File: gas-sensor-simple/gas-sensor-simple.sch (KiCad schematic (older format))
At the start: 31 parts, among them J1 6-pin male, J2 6-pin female, J3 8-pin male, U1 MQ-8, U10 MV5x3x, U11 MV5x3x, U12 LM393, U13 ads1x15, U14 ads1x15, U15 BME280, U2 MQ-4, U3 CO2, U4 O2, U5 7407, U6 7407, U8 MV5x3x, U9 MV5x3x

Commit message: Begin PCB layout.
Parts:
- removed J1: 6-pin male, symbol Conn_01x06_Male
- removed J2: 6-pin female, symbol Conn_01x06_Female
- added unit 2 of U12
- added unit 5 of U5
- added unit 6 of U5
- added unit 5 of U6
- added unit 6 of U6
- J1: renamed from J3; footprint (none) -> Pin_Headers:Pin_Header_Straight_1x08_Pitch2.54mm
- R1, R2, R3, R4, R5, R6, R7, R8: footprint (none) -> Resistors_THT:R_Axial_DIN0207_L6.3mm_D2.5mm_P10.16mm_Horizontal
- RV1: footprint (none) -> Potentiometers:Potentiometer_Trimmer_Piher_PT-10h5_Vertical_Px5.0mm_Py5.0mm
- TH1, TH2, TH3, TH4: footprint (none) -> Resistors_THT:R_Axial_DIN0204_L3.6mm_D1.6mm_P7.62mm_Horizontal
- U1, U2, U4: footprint (none) -> Socket_Strips:Socket_Strip_Straight_1x04_Pitch2.54mm
- U10, U11, U8, U9: footprint (none) -> Socket_Strips:Socket_Strip_Straight_1x03_Pitch2.54mm
- U12: footprint (none) -> Housings_DIP:DIP-8_W7.62mm
- U13, U14: footprint (none) -> Socket_Strips:Socket_Strip_Straight_1x10_Pitch2.54mm
- U15: footprint (none) -> Housings_DIP:DIP-12_W10.16mm
- U3: footprint (none) -> Pin_Headers:Pin_Header_Straight_1x04_Pitch2.54mm
- U5, U6: footprint (none) -> Housings_DIP:DIP-14_W7.62mm
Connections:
- wire segments 170 -> 163
- no-connect marks 6 -> 13
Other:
- note removed: "(5V)"

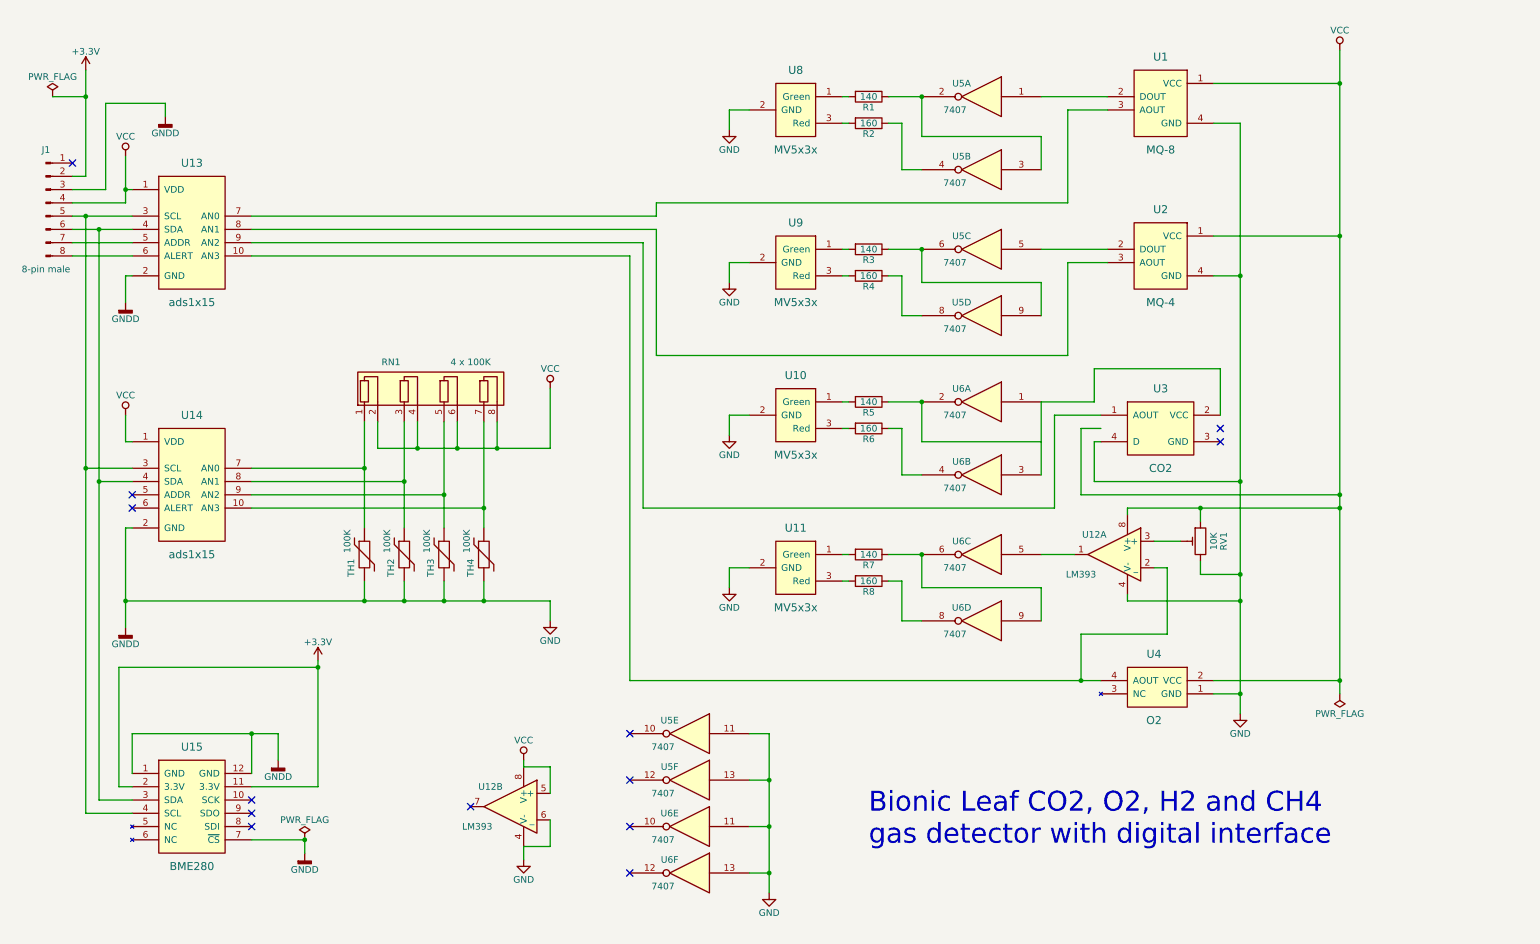
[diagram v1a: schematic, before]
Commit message: Add back headers to separate analog board from digital.
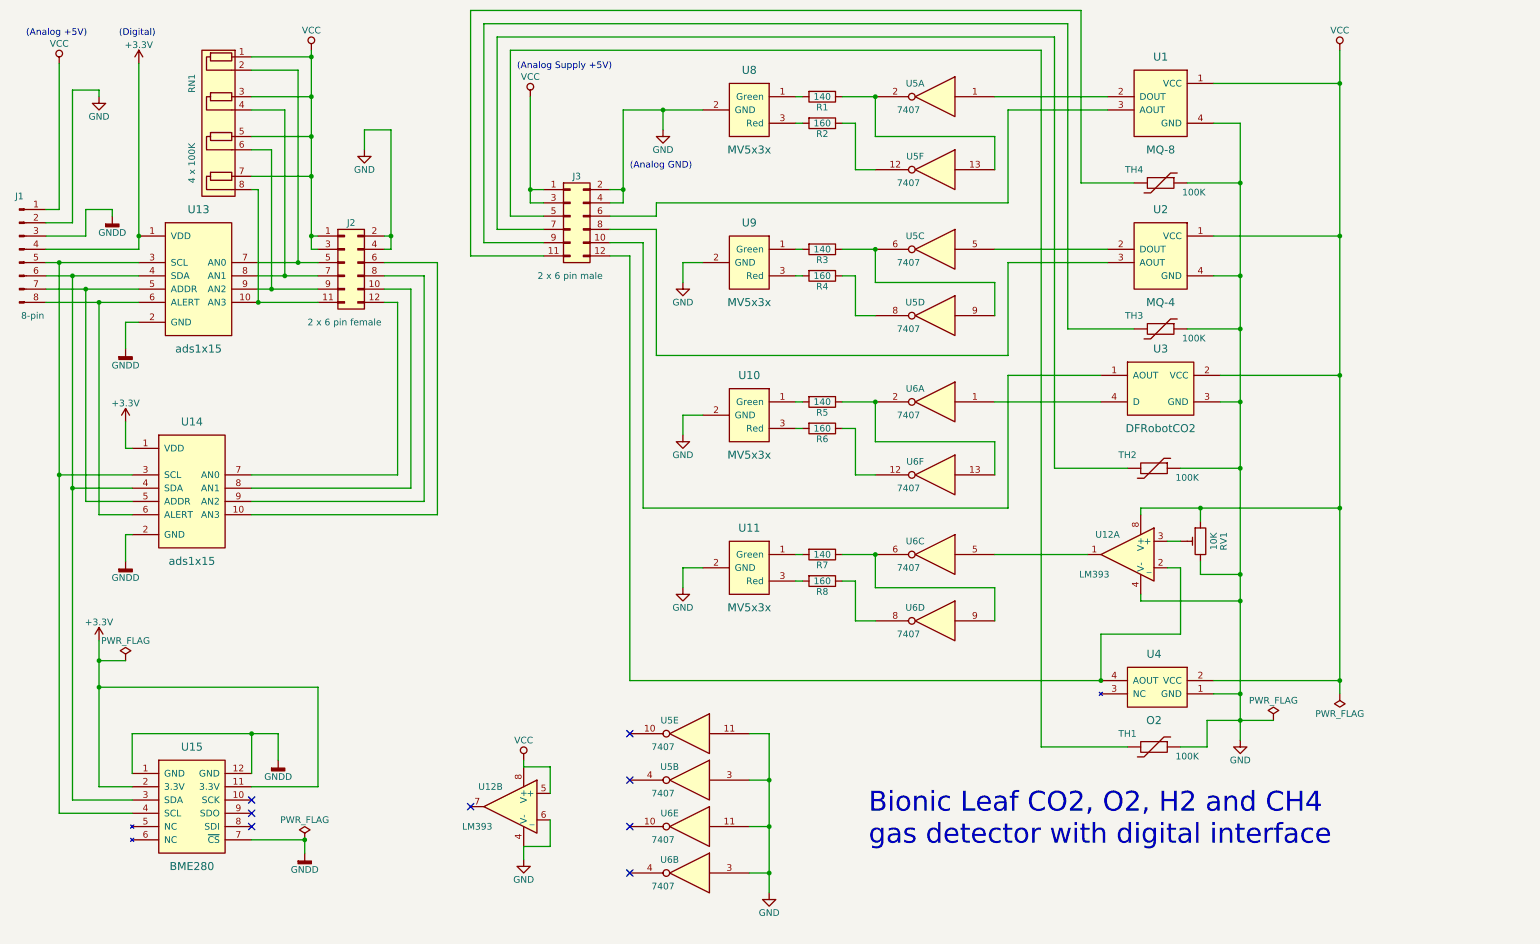
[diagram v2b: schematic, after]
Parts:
- added J2: 2 x 6 pin female, Socket_Strips:Socket_Strip_Straight_2x06_Pitch2.54mm, symbol Conn_02x06_Odd_Even
- added J3: 2 x 6 pin male, Pin_Headers:Pin_Header_Straight_2x06_Pitch2.54mm, symbol Conn_02x06_Odd_Even
- J1: value 8-pin male -> 8-pin
- TH1, TH2, TH3, TH4: footprint Resistors_THT:R_Axial_DIN0204_L3.6mm_D1.6mm_P7.62mm_Horizontal -> Socket_Strips:Socket_Strip_Straight_1x02_Pitch2.54mm
- U3: value CO2 -> DFRobotCO2; footprint Pin_Headers:Pin_Header_Straight_1x04_Pitch2.54mm -> Socket_Strips:Socket_Strip_Straight_1x04_Pitch2.54mm
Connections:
- net +3V3: now also J1.4 (Pin_4), U13.1 (VDD), U14.1 (VDD); no longer J1.2 (Pin_2)
- net GND: now also J1.2 (Pin_2), TH1.1, TH2.1, TH3.1, TH4.1, U3.3 (GND), U5.3, U6.3, J2.2 (Pin_2), J2.4 (Pin_4), J3.2 (Pin_2), J3.4 (Pin_4); no longer J1.3 (Pin_3), TH1.2, TH2.2, TH3.2, TH4.2, U13.2 (GND), U14.2 (GND), U15.1 (GND), U15.12 (GND), U15.7 (~CS~), U3.4 (D), U5.13, U6.13
- net VCC: now also J1.1 (Pin_1), RN1.1 (R1.1), RN1.3 (R2.1), RN1.5 (R3.1), RN1.7 (R4.1), U3.2 (VCC), J2.1 (Pin_1), J2.3 (Pin_3), J3.1 (Pin_1), J3.3 (Pin_3); no longer J1.4 (Pin_4), RN1.2 (R1.2), RN1.4 (R2.2), RN1.6 (R3.2), RN1.8 (R4.2), U13.1 (VDD), U14.1 (VDD)
- net at U1.3 (AOUT): now also J3.6 (Pin_6); no longer U13.7 (AN0)
- net at U2.3 (AOUT): now also J3.8 (Pin_8); no longer U13.8 (AN1)
- net at J1.7 (Pin_7), U13.5 (ADDR): now also U14.5 (ADDR)
- net at J1.8 (Pin_8), U13.6 (ALERT): now also U14.6 (ALERT)
- net at R1.1, U5.2: now also U5.13; no longer U5.3
- net at R2.1: now also U5.12; no longer U5.4
- net at R5.1, U6.2: now also U6.13
- net at R6.1: now also U6.12; no longer U6.4
- net at U12.2 (_), U4.4 (AOUT): now also J3.12 (Pin_12); no longer U13.10 (AN3)
- net at U13.9 (AN2): now also RN1.6 (R3.2), J2.9 (Pin_9); no longer U3.1 (AOUT)
- new net: U3.4 (D), U6.1
- new net: J2.11 (Pin_11), RN1.8 (R4.2), U13.10 (AN3)
- new net: J2.5 (Pin_5), RN1.2 (R1.2), U13.7 (AN0)
- new net: J2.7 (Pin_7), RN1.4 (R2.2), U13.8 (AN1)
- new net: J2.6 (Pin_6), U14.10 (AN3)
- new net: J2.12 (Pin_12), U14.7 (AN0)
- new net: J2.10 (Pin_10), U14.8 (AN1)
- new net: J2.8 (Pin_8), U14.9 (AN2)
- new net: J3.5 (Pin_5), TH1.2
- new net: J3.7 (Pin_7), TH2.2
- new net: J3.9 (Pin_9), TH3.2
- new net: J3.11 (Pin_11), TH4.2
- new net: J3.10 (Pin_10), U3.1 (AOUT)
- new net GNDD: J1.3 (Pin_3), U13.2 (GND), U14.2 (GND), U15.1 (GND), U15.12 (GND), U15.7 (~CS~)
- no-connect marks 13 -> 8
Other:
- note added: "(Analog +5V)"
- note added: "(Analog GND)"
- note added: "(Analog Supply +5V)"
- note added: "(Digital)"
- moved on the sheet: J1, R1, R2, R3, R4, R5, R6, R7, R8, RN1, TH1, TH2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

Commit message: Start adding capacitors and improve PCB layout.
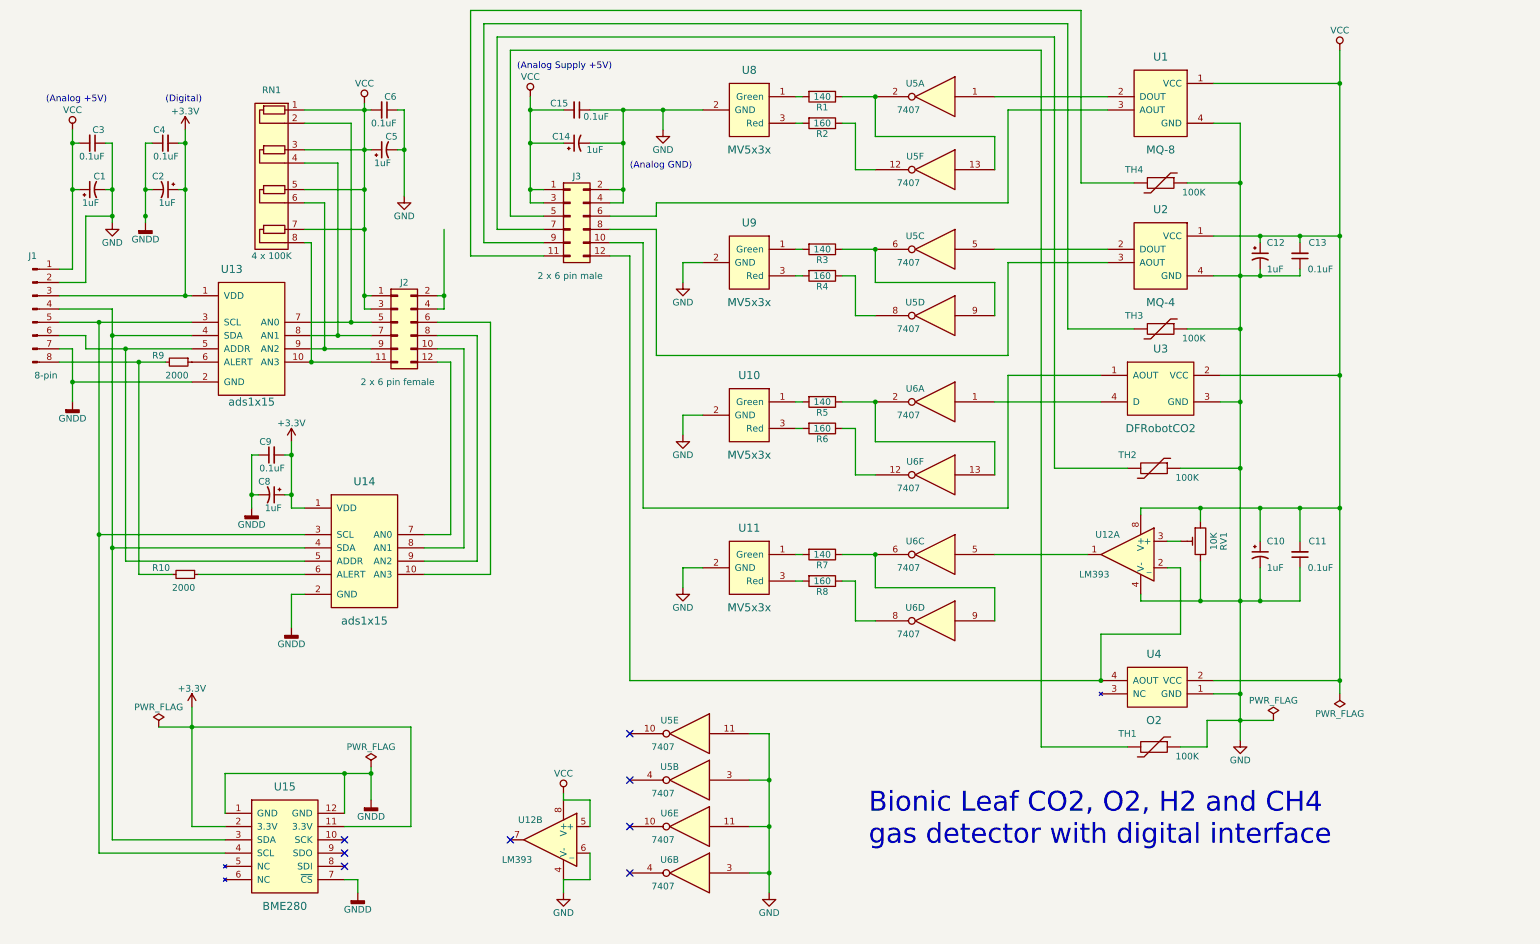
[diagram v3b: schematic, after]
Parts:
- added C1, C2, C5, C8: 1uF, Capacitors_THT:CP_Radial_D5.0mm_P2.50mm, symbol CP1_Small
- added C10, C12, C14: 1uF, symbol CP1_Small
- added C11, C13, C15: 0.1uF, symbol C_Small
- added C3, C4, C6, C9: 0.1uF, Capacitors_THT:C_Disc_D5.0mm_W2.5mm_P2.50mm, symbol C_Small
- added R10, R9: 2000, symbol R_Small
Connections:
- net +3V3: now also J1.3 (Pin_3), C2.1, C4.2, C8.1, C9.2; no longer J1.4 (Pin_4)
- net GND: now also C1.2, C10.2, C11.1, C12.2, C13.1, C14.2, C15.1, C3.1, C5.2, C6.1; no longer J2.2 (Pin_2), J2.4 (Pin_4)
- net GNDD: now also J1.7 (Pin_7), C2.2, C4.1, C8.2, C9.1; no longer J1.3 (Pin_3)
- net VCC: now also C1.1, C10.1, C11.2, C12.1, C13.2, C14.1, C15.2, C3.2, C5.1, C6.2
- net at U13.4 (SDA), U14.4 (SDA), U15.3 (SDA): now also J1.4 (Pin_4); no longer J1.6 (Pin_6)
- net at U13.5 (ADDR), U14.5 (ADDR): now also J1.6 (Pin_6); no longer J1.7 (Pin_7)
- new net: J1.8 (Pin_8), R10.2, R9.2
- new net: R9.1, U13.6 (ALERT)
- new net: R10.1, U14.6 (ALERT)
- new net: J2.2 (Pin_2), J2.4 (Pin_4)
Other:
- moved on the sheet: J1, J2, RN1, U12B, U13, U14, U15

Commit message: Autorouted version 1 (gas-sensor-simple.kicad_pcb). Start work on version 2 layout (layout.kicad_pcb) moving RPi connector to top of digital board.
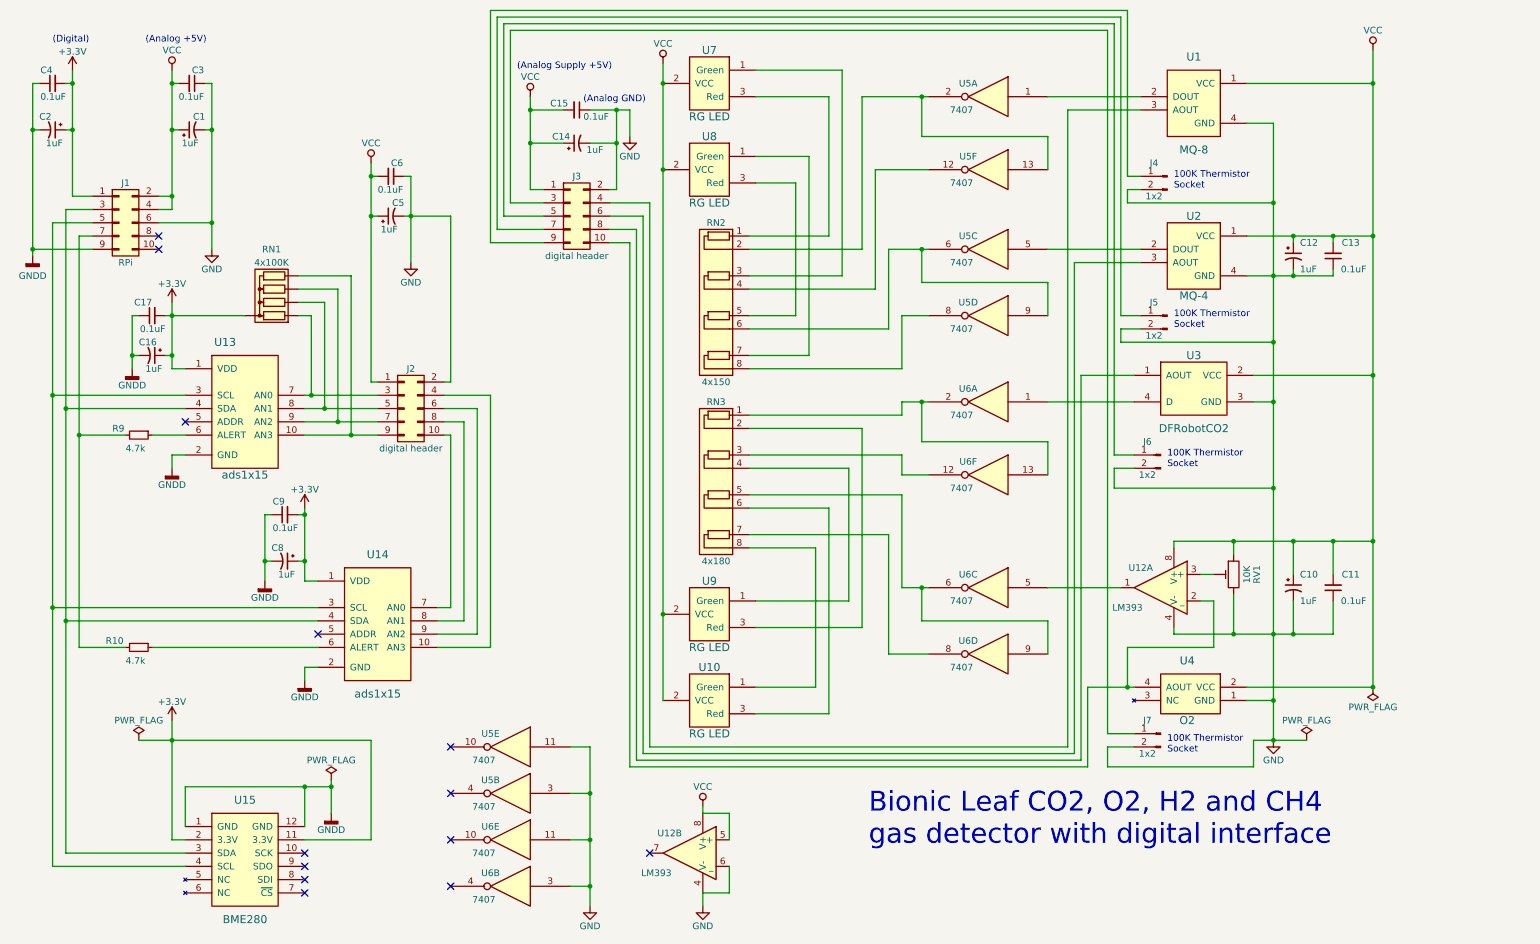
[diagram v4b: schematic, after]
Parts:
- removed J1: 8-pin, Pin_Headers:Pin_Header_Straight_1x08_Pitch2.54mm, symbol Conn_01x08_Male
- removed J2: 2 x 6 pin female, Socket_Strips:Socket_Strip_Straight_2x06_Pitch2.54mm, symbol Conn_02x06_Odd_Even
- removed J3: 2 x 6 pin male, Pin_Headers:Pin_Header_Straight_2x06_Pitch2.54mm, symbol Conn_02x06_Odd_Even
- removed R1, R3, R5, R7: 140, Resistors_THT:R_Axial_DIN0207_L6.3mm_D2.5mm_P10.16mm_Horizontal, symbol R
- removed R2, R4, R6, R8: 160, Resistors_THT:R_Axial_DIN0207_L6.3mm_D2.5mm_P10.16mm_Horizontal, symbol R
- removed RN1: 4 x 100K, Resistors_THT:R_Array_SIP8, symbol R_Pack04_SIP
- removed TH1, TH2, TH3, TH4: 100K, Socket_Strips:Socket_Strip_Straight_1x02_Pitch2.54mm, symbol Thermistor
- removed U10, U11, U8, U9: MV5x3x, Socket_Strips:Socket_Strip_Straight_1x03_Pitch2.54mm, symbol MV5x3x
- added C16: 1uF, Capacitors_THT:CP_Radial_D5.0mm_P2.00mm, symbol CP1_Small
- added C17: 0.1uF, Capacitors_THT:C_Disc_D5.0mm_W2.5mm_P2.50mm, symbol C_Small
- added J1: RPi, Pin_Headers:Pin_Header_Straight_2x05_Pitch2.54mm, symbol Conn_02x05_Odd_Even
- added J2: digital header, Socket_Strips:Socket_Strip_Straight_2x05_Pitch2.54mm, symbol Conn_02x05_Odd_Even
- added J3: digital header, Pin_Headers:Pin_Header_Straight_2x05_Pitch2.54mm, symbol Conn_02x05_Odd_Even
- added J4, J5, J6, J7: 1x2, Pin_Headers:Pin_Header_Straight_1x02_Pitch2.54mm, symbol Conn_01x02_Male
- added RN1: 4x100K, Resistors_THT:R_Array_SIP5, symbol R_Network04
- added RN2: 4x150, Resistors_THT:R_Array_SIP8, symbol R_Pack04_SIP
- added RN3: 4x180, Resistors_THT:R_Array_SIP8, symbol R_Pack04_SIP
- added U10, U7, U8, U9: RG LED, Socket_Strips:Socket_Strip_Straight_1x03_Pitch2.54mm, symbol ComAnode
- C1, C2, C5, C8: footprint Capacitors_THT:CP_Radial_D5.0mm_P2.50mm -> Capacitors_THT:CP_Radial_D5.0mm_P2.00mm
- C10, C12, C14: footprint (none) -> Capacitors_THT:CP_Radial_D5.0mm_P2.00mm
- C11, C13, C15: footprint (none) -> Capacitors_THT:C_Disc_D5.0mm_W2.5mm_P2.50mm
- R10, R9: value 2000 -> 4.7k; footprint (none) -> Resistors_THT:R_Axial_DIN0207_L6.3mm_D2.5mm_P10.16mm_Horizontal
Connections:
- net +3V3: now also C16.1, C17.2, J1.1 (Pin_1), RN1.1 (common)
- net GND: now also J1.6 (Pin_6), J2.2 (Pin_2), J3.2 (Pin_2), J4.2 (Pin_2), J5.2 (Pin_2), J6.2 (Pin_2), J7.2 (Pin_2)
- net GNDD: now also C16.2, C17.1, J1.9 (Pin_9); no longer U15.7 (~CS~)
- net VCC: now also J1.2 (Pin_2), J1.4 (Pin_4), J2.1 (Pin_1), J3.1 (Pin_1), U10.2 (VCC), U7.2 (VCC), U8.2 (VCC), U9.2 (VCC)
- net at U1.3 (AOUT): now also J3.4 (Pin_4)
- net at U2.3 (AOUT): now also J3.6 (Pin_6)
- net at U13.4 (SDA), U14.4 (SDA), U15.3 (SDA): now also J1.3 (Pin_3)
- net at U13.3 (SCL), U14.3 (SCL), U15.4 (SCL): now also J1.5 (Pin_5)
- net at U13.5 (ADDR): no longer U14.5 (ADDR)
- net at R10.2, R9.2: now also J1.7 (Pin_7)
- net at U5.13, U5.2: now also RN2.2 (R1.2)
- net at U5.12: now also RN2.4 (R2.2)
- net at U5.6, U5.9: now also RN2.6 (R3.2)
- net at U5.8: now also RN2.8 (R4.2)
- net at U6.13, U6.2: now also RN3.1 (R1.1)
- net at U6.12: now also RN3.3 (R2.1)
- net at U6.6, U6.9: now also RN3.5 (R3.1)
- net at U6.8: now also RN3.7 (R4.1)
- net at U13.10 (AN3): now also J2.9 (Pin_9), RN1.5 (R4)
- net at U13.7 (AN0): now also J2.3 (Pin_3), RN1.2 (R1)
- net at U13.8 (AN1): now also J2.5 (Pin_5), RN1.3 (R2)
- net at U13.9 (AN2): now also J2.7 (Pin_7), RN1.4 (R3)
- net at U14.10 (AN3): now also J2.4 (Pin_4)
- net at U14.7 (AN0): now also J2.10 (Pin_10)
- net at U14.8 (AN1): now also J2.8 (Pin_8)
- net at U14.9 (AN2): now also J2.6 (Pin_6)
- net at U12.2 (_), U4.4 (AOUT): now also J3.10 (Pin_10)
- net at U3.1 (AOUT): now also J3.8 (Pin_8)
- new net: J3.3 (Pin_3), J7.1 (Pin_1)
- new net: J3.5 (Pin_5), J6.1 (Pin_1)
- new net: J3.7 (Pin_7), J5.1 (Pin_1)
- new net: J3.9 (Pin_9), J4.1 (Pin_1)
- new net: RN2.1 (R1.1), U7.3 (Red)
- new net: RN2.3 (R2.1), U7.1 (Green)
- new net: RN2.5 (R3.1), U8.3 (Red)
- new net: RN2.7 (R4.1), U8.1 (Green)
- new net: RN3.2 (R1.2), U9.3 (Red)
- new net: RN3.4 (R2.2), U9.1 (Green)
- new net: RN3.6 (R3.2), U10.3 (Red)
- new net: RN3.8 (R4.2), U10.1 (Green)
- no-connect marks 8 -> 13
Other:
- note added: "100K Thermistor\nSocket"
- moved on the sheet: C1, C10, C11, C12, C13, C2, C3, C4, C5, C6, C8, C9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
